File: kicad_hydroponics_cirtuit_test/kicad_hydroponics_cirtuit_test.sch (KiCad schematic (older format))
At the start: 8 parts, among them Q1 IRLZ34N

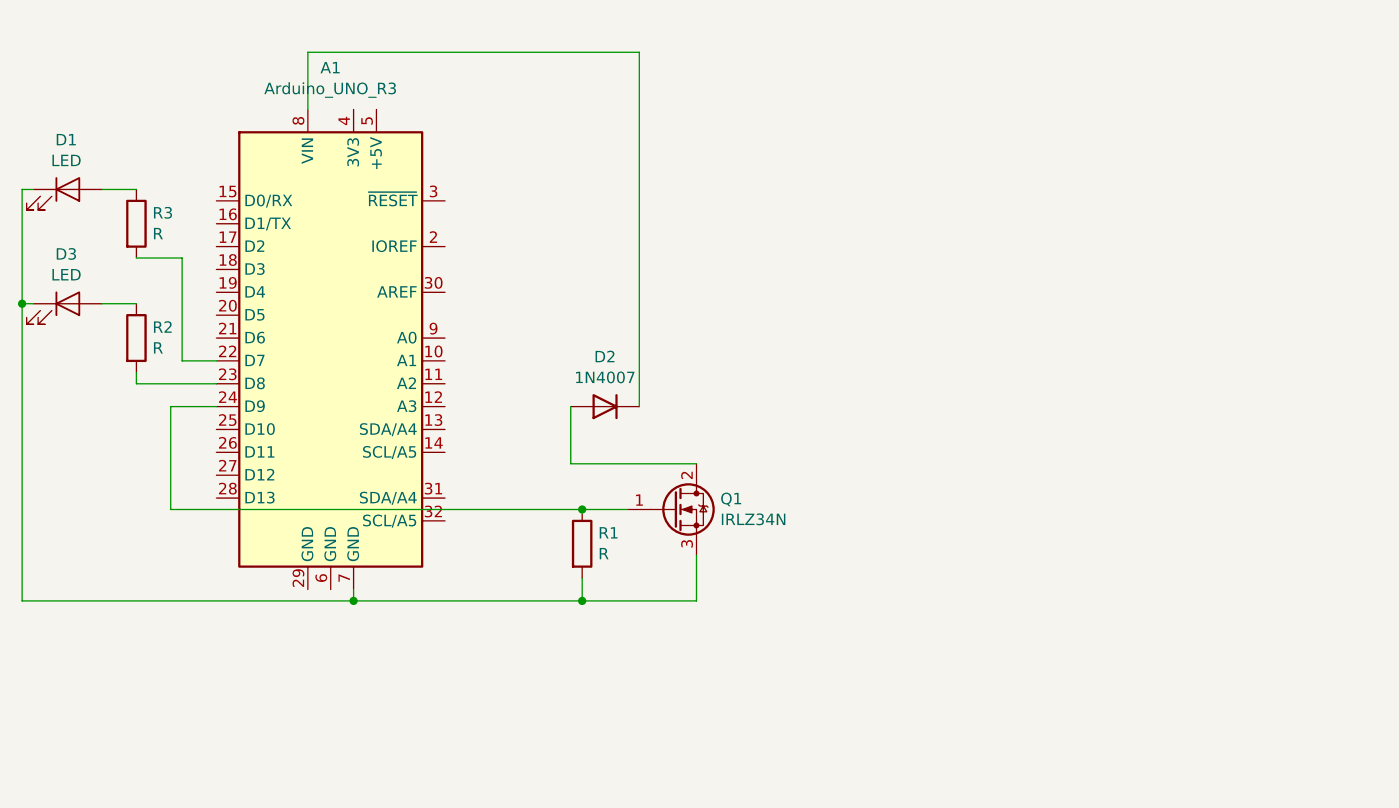
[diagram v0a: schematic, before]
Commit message: Updated to use SMD components except diode 1N4007 is through hole. Water level sensor powering from Arduino digital pins to prevent sensor electrochemical corrosion
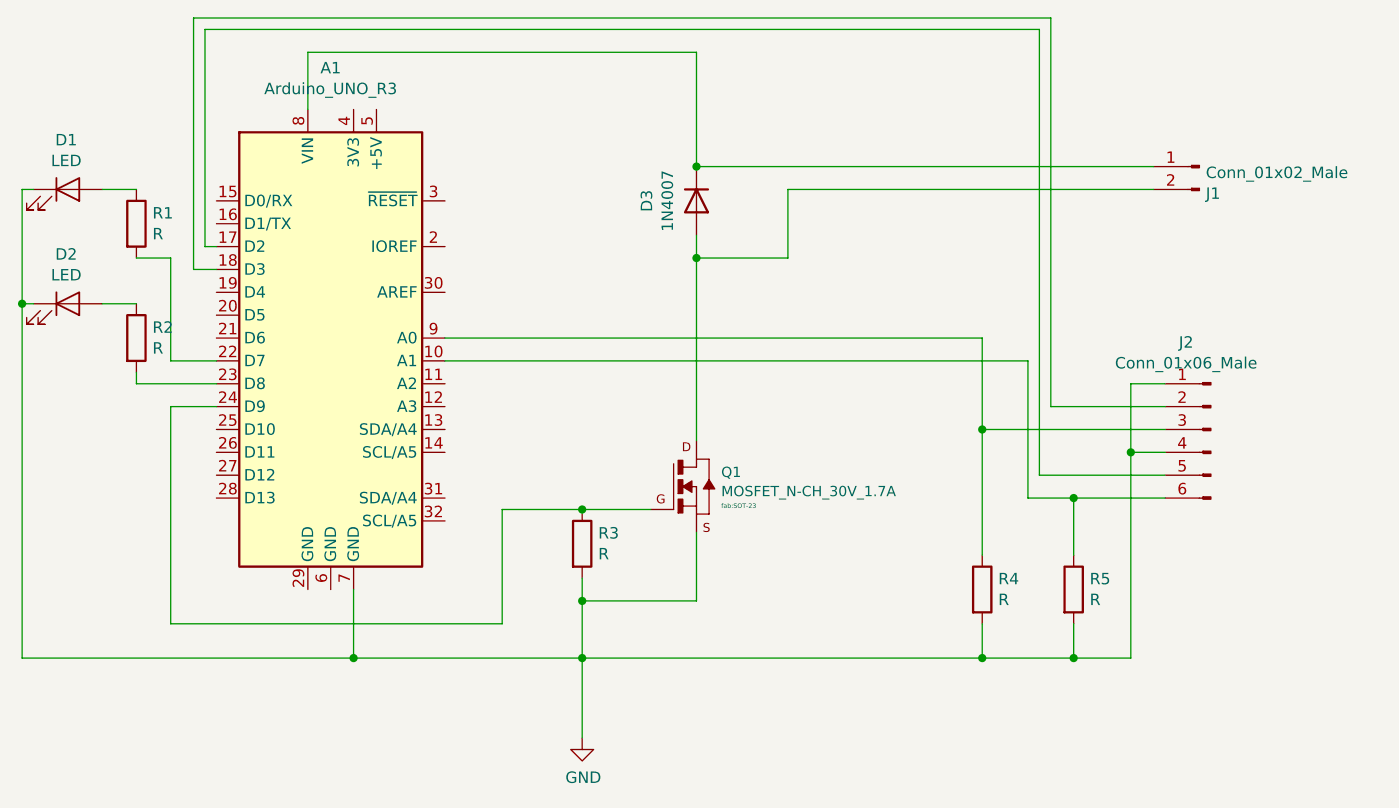
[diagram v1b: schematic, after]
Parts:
- removed Q1: IRLZ34N, Package_TO_SOT_THT:TO-220-3_Vertical, symbol Transistor_FET:IRLZ34N
- added J1: Conn_01x02_Male, fab:Header_SMD_01x02_P2.54mm_Horizontal_Male, symbol fab:Conn_01x02_Male
- added J2: Conn_01x06_Male, fab:Header_SMD_01x06_P2.54mm_Horizontal_Male, symbol fab:Conn_01x06_Male
- added Q1: MOSFET_N-CH_30V_1.7A, fab:SOT-23, symbol fab:MOSFET_N-CH_30V_1.7A
- added R4, R5: R, fab:R_1206, symbol fab:R
- renumbered D3 to D2, D2 to D3, R3 to R1, R1 to R3
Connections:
- net at A1.10 (A1): now also J2.6 (Pin_6), R5.1
- net at A1.17 (D2): now also J2.5 (Pin_5)
- net at A1.18 (D3): now also J2.2 (Pin_2)
- net at A1.24 (D9), R3.1: now also Q1.1 (G)
- net GND: now reaches A1.7 (GND), D1.1 (K), D2.1 (K), R3.2
- net GND: now also J2.1 (Pin_1), J2.4 (Pin_4), Q1.2 (S), R4.2, R5.2
- net at A1.8 (VIN), D3.1 (K): now also J1.1 (Pin_1)
- net at A1.9 (A0): now also J2.3 (Pin_3), R4.1
- net at D3.2 (A): now also J1.2 (Pin_2), Q1.3 (D)
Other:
- moved on the sheet: D3
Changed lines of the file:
@@
 $EndDescr
 $Comp
-L Transistor_FET:IRLZ34N Q1
-U 1 1 60748F81
-P 6950 3350
-F 0 "Q1" H 7154 3396 50  0000 L CNN
-F 1 "IRLZ34N" H 7154 3305 50  0000 L CNN
-F 2 "Package_TO_SOT_THT:TO-220-3_Vertical" H 7200 3275 50  0001 L CIN
-F 3 "http://www.infineon.com/dgdl/irlz34npbf.pdf?fileId=5546d462533600a40153567206892720" H 6950 3350 50  0001 L CNN
-	1    6950 3350
-	1    0    0    -1
-$EndComp
-$Comp
-L Diode:1N4007 D2
-U 1 1 6074A480
-P 6650 2900
-F 0 "D2" H 6650 2683 50  0000 C CNN
-F 1 "1N4007" H 6650 2774 50  0000 C CNN
-F 2 "Diode_THT:D_DO-41_SOD81_P10.16mm_Horizontal" H 6650 2725 50  0001 C CNN
-F 3 "http://www.vishay.com/docs/88503/1n4001.pdf" H 6650 2900 50  0001 C CNN
-	1    6650 2900
-	-1   0    0    1
-$EndComp
-$Comp
-L fab:R R3
+L fab:R R1
 U 1 1 60752E1F
 P 4600 2100
-F 0 "R3" H 4670 2146 50  0000 L CNN
+F 0 "R1" H 4670 2146 50  0000 L CNN
 F 1 "R" H 4670 2055 50  0000 L CNN
 F 2 "fab:R_1206" V 4530 2100 50  0001 C CNN
@@
 $EndComp
 $Comp
-L fab:LED D3
+L fab:LED D2
 U 1 1 60755A04
 P 4300 2450
-F 0 "D3" H 4293 2666 50  0000 C CNN
+F 0 "D2" H 4293 2666 50  0000 C CNN
 F 1 "LED" H 4293 2575 50  0000 C CNN
 F 2 "fab:LED_1206" H 4300 2450 50  0001 C CNN
@@
 $EndComp
 $Comp
-L fab:R R1
+L fab:R R3
 U 1 1 60756A6C
 P 6550 3500
-F 0 "R1" H 6620 3546 50  0000 L CNN
+F 0 "R3" H 6620 3546 50  0000 L CNN
 F 1 "R" H 6620 3455 50  0000 L CNN
 F 2 "fab:R_1206" V 6480 3500 50  0001 C CNN
@@
 $EndComp
 Wire Wire Line
-	4750 3350 4750 2900
-Wire Wire Line
 	4750 2900 4950 2900
 Wire Wire Line
@@
 	4600 2450 4450 2450
 Wire Wire Line
-	4600 2250 4800 2250
-Wire Wire Line
-	4800 2250 4800 2700
-Wire Wire Line
-	4800 2700 4950 2700
+	4600 2250 4750 2250
 Wire Wire Line
 	4600 2750 4600 2800
@@
 Wire Wire Line
 	4150 2450 4100 2450
-Wire Wire Line
-	4100 2450 4100 3750
-Wire Wire Line
-	4100 3750 5550 3750
-Wire Wire Line
-	5550 3750 5550 3700
 Wire Wire Line
 	4150 1950 4100 1950
@@
 Connection ~ 4100 2450
 Wire Wire Line
-	7050 3550 7050 3750
-Wire Wire Line
 	7050 3750 6550 3750
-Connection ~ 5550 3750
 Wire Wire Line
 	6550 3650 6550 3750
+Wire Wire Line
+	5350 1350 5350 1600
+$Comp
+L fab:MOSFET_N-CH_30V_1.7A Q1
+U 1 1 607F16BB
+P 7050 3250
+F 0 "Q1" H 7158 3313 45  0000 L CNN
+F 1 "MOSFET_N-CH_30V_1.7A" H 7158 3229 45  0000 L CNN
+F 2 "fab:SOT-23" H 7158 3166 20  0000 L CNN
+F 3 "https://www.onsemi.com/pub/Collateral/NDS355AN-D.PDF" H 7050 3250 50  0001 C CNN
+	1    7050 3250
+	1    0    0    -1
+$EndComp
+Wire Wire Line
+	6550 3350 6850 3350
+Wire Wire Line
+	7050 3450 7050 3750
+$Comp
+L fab:R R4
+U 1 1 607FD04D
+P 8300 3700
+F 0 "R4" H 8370 3746 50  0000 L CNN
+F 1 "R" H 8370 3655 50  0000 L CNN
+F 2 "fab:R_1206" V 8230 3700 50  0001 C CNN
+F 3 "~" H 8300 3700 50  0001 C CNN
+	1    8300 3700
+	1    0    0    -1
+$EndComp
+$Comp
+L fab:R R5
+U 1 1 607FDECE
+P 8700 3700
+F 0 "R5" H 8770 3746 50  0000 L CNN
+F 1 "R" H 8770 3655 50  0000 L CNN
+F 2 "fab:R_1206" V 8630 3700 50  0001 C CNN
+F 3 "~" H 8700 3700 50  0001 C CNN
+	1    8700 3700
+	1    0    0    -1
+$EndComp
+Wire Wire Line
+	8700 4000 8700 3850
+Wire Wire Line
+	8300 3850 8300 4000
+$Comp
+L fab:Conn_01x06_Male J2
+U 1 1 6080111E
+P 9300 3000
+F 0 "J2" H 9408 3381 50  0000 C CNN
+F 1 "Conn_01x06_Male" H 9408 3290 50  0000 C CNN
+F 2 "fab:Header_SMD_01x06_P2.54mm_Horizontal_Male" H 9300 3000 50  0001 C CNN
+F 3 "~" H 9300 3000 50  0001 C CNN
+	1    9300 3000
+	-1   0    0    -1
+$EndComp
+Wire Wire Line
+	9100 3300 8700 3300
+Wire Wire Line
+	8700 3300 8700 3550
+Wire Wire Line
+	9100 3000 8300 3000
+Wire Wire Line
+	8300 3000 8300 3550
+Wire Wire Line
+	9100 2800 8950 2800
+Wire Wire Line
+	8950 2800 8950 3100
+Wire Wire Line
+	8950 4000 8700 4000
+Connection ~ 8700 4000
+Wire Wire Line
+	9100 3100 8950 3100
+Connection ~ 8950 3100
+Wire Wire Line
+	8950 3100 8950 4000
+$Comp
+L fab:Conn_01x02_Male J1
+U 1 1 608116CF
+P 9250 1850
+F 0 "J1" H 9222 1732 50  0000 R CNN
+F 1 "Conn_01x02_Male" H 9222 1823 50  0000 R CNN
+F 2 "fab:Header_SMD_01x02_P2.54mm_Horizontal_Male" H 9250 1850 50  0001 C CNN
+F 3 "~" H 9250 1850 50  0001 C CNN
+	1    9250 1850
+	-1   0    0    -1
+$EndComp
+Wire Wire Line
+	7050 1350 7050 1850
+Wire Wire Line
+	5350 1350 7050 1350
+Wire Wire Line
+	9050 1950 7450 1950
+Wire Wire Line
+	4100 2450 4100 4000
+Wire Wire Line
+	6550 3750 6550 4000
 Connection ~ 6550 3750
 Wire Wire Line
-	6550 3750 5550 3750
-Wire Wire Line
-	4750 3350 6550 3350
+	6200 3850 6200 3350
+Wire Wire Line
+	6200 3350 6550 3350
+Wire Wire Line
+	4750 2900 4750 3850
 Connection ~ 6550 3350
 Wire Wire Line
-	6550 3350 6750 3350
-Wire Wire Line
-	7050 3150 6500 3150
-Wire Wire Line
-	6500 3150 6500 2900
-Wire Wire Line
-	6800 2900 6800 1350
-Wire Wire Line
-	6800 1350 5350 1350
-Wire Wire Line
-	5350 1350 5350 1600
+	7050 2150 7050 2250
+Wire Wire Line
+	7450 2250 7050 2250
+Connection ~ 7050 2250
+Wire Wire Line
+	7050 2250 7050 3050
+Wire Wire Line
+	7450 1950 7450 2250
+Connection ~ 8300 3000
+Wire Wire Line
+	8500 3300 8700 3300
+Connection ~ 8700 3300
+Connection ~ 7050 1850
+$Comp
+L Diode:1N4007 D3
+U 1 1 6074A480
+P 7050 2000
+F 0 "D3" H 7050 1783 50  0000 C CNN
+F 1 "1N4007" H 7050 1874 50  0000 C CNN
+F 2 "Diode_THT:D_DO-41_SOD81_P10.16mm_Horizontal" H 7050 1825 50  0001 C CNN
+F 3 "http://www.vishay.com/docs/88503/1n4001.pdf" H 7050 2000 50  0001 C CNN
+	1    7050 2000
+	0    1    1    0
+$EndComp
+Wire Wire Line
+	8300 4000 8700 4000
+Wire Wire Line
+	5950 2600 8300 2600
+Wire Wire Line
+	8300 2600 8300 3000
+Wire Wire Line
+	5950 2700 8500 2700
+Wire Wire Line
+	8500 2700 8500 3300
+Wire Wire Line
+	6550 4000 8300 4000
+Connection ~ 6550 4000
+Connection ~ 8300 4000
+Wire Wire Line
+	7050 1850 9050 1850
+Wire Wire Line
+	9100 3200 8550 3200
+Wire Wire Line
+	8550 3200 8550 1250
+Wire Wire Line
+	8550 1250 4900 1250
+Wire Wire Line
+	4900 1250 4900 2200
+Wire Wire Line
+	4900 2200 4950 2200
+Wire Wire Line
+	4750 2250 4750 2700
+Wire Wire Line
+	4750 2700 4950 2700
+Wire Wire Line
+	4950 2300 4850 2300
+Wire Wire Line
+	4850 2300 4850 1200
+Wire Wire Line
+	4850 1200 8600 1200
+Wire Wire Line
+	8600 1200 8600 2900
+Wire Wire Line
+	8600 2900 9100 2900
+Wire Wire Line
+	6200 3850 4750 3850
+Wire Wire Line
+	5550 3700 5550 4000
+Connection ~ 5550 4000
+Wire Wire Line
+	5550 4000 6550 4000
+$Comp
+L power:GND #PWR0101
+U 1 1 608146A2
+P 6550 4350
+F 0 "#PWR0101" H 6550 4100 50  0001 C CNN
+F 1 "GND" H 6555 4177 50  0000 C CNN
+F 2 "" H 6550 4350 50  0001 C CNN
+F 3 "" H 6550 4350 50  0001 C CNN
+	1    6550 4350
+	1    0    0    -1
+$EndComp
+Wire Wire Line
+	6550 4350 6550 4000
+Wire Wire Line
+	4100 4000 5550 4000
 $EndSCHEMATC
